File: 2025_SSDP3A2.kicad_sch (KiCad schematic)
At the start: 63 parts, among them J1 SolderPad, J2 SolderPad, J3 SolderPad, J4 SolderPad, Q1 CSD19534Q5A, Q2 BSC0805LS, U1 LM5146RGYR

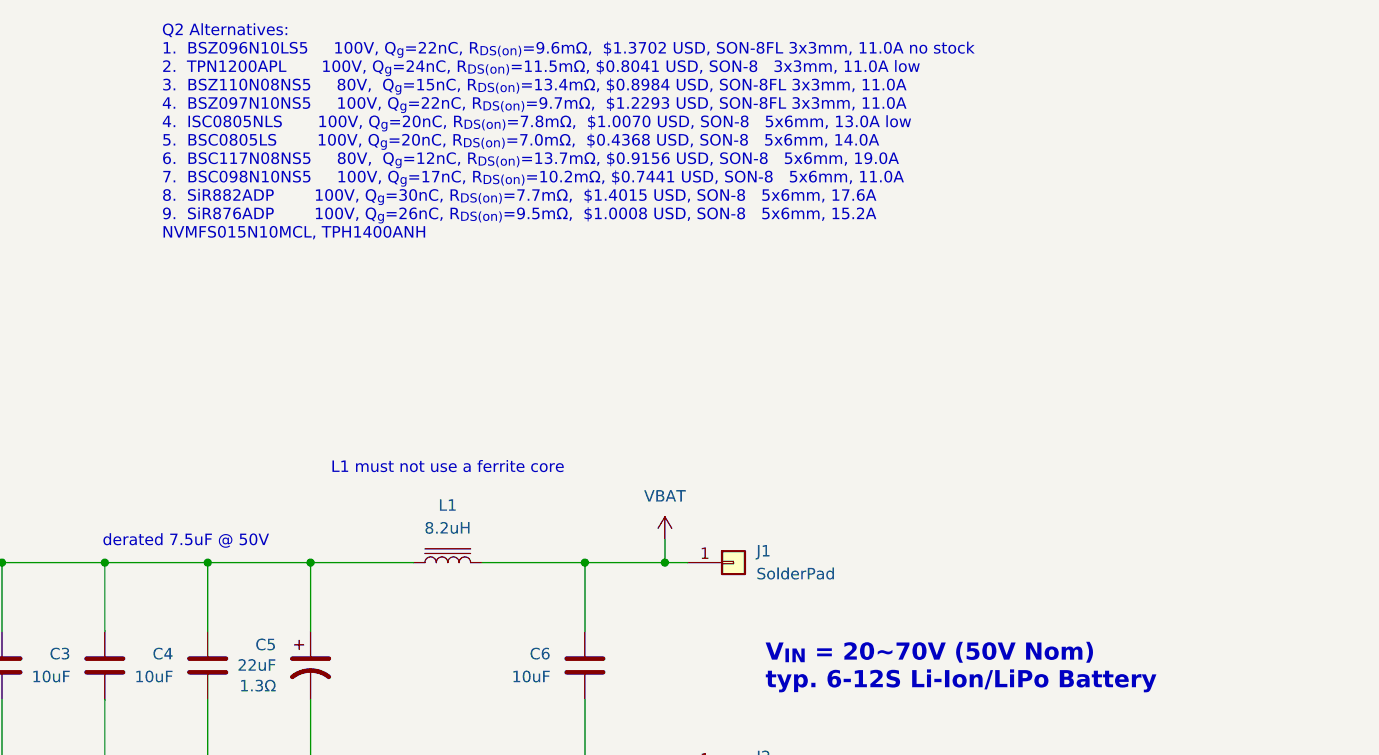
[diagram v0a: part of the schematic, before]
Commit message: Revised PCB layout
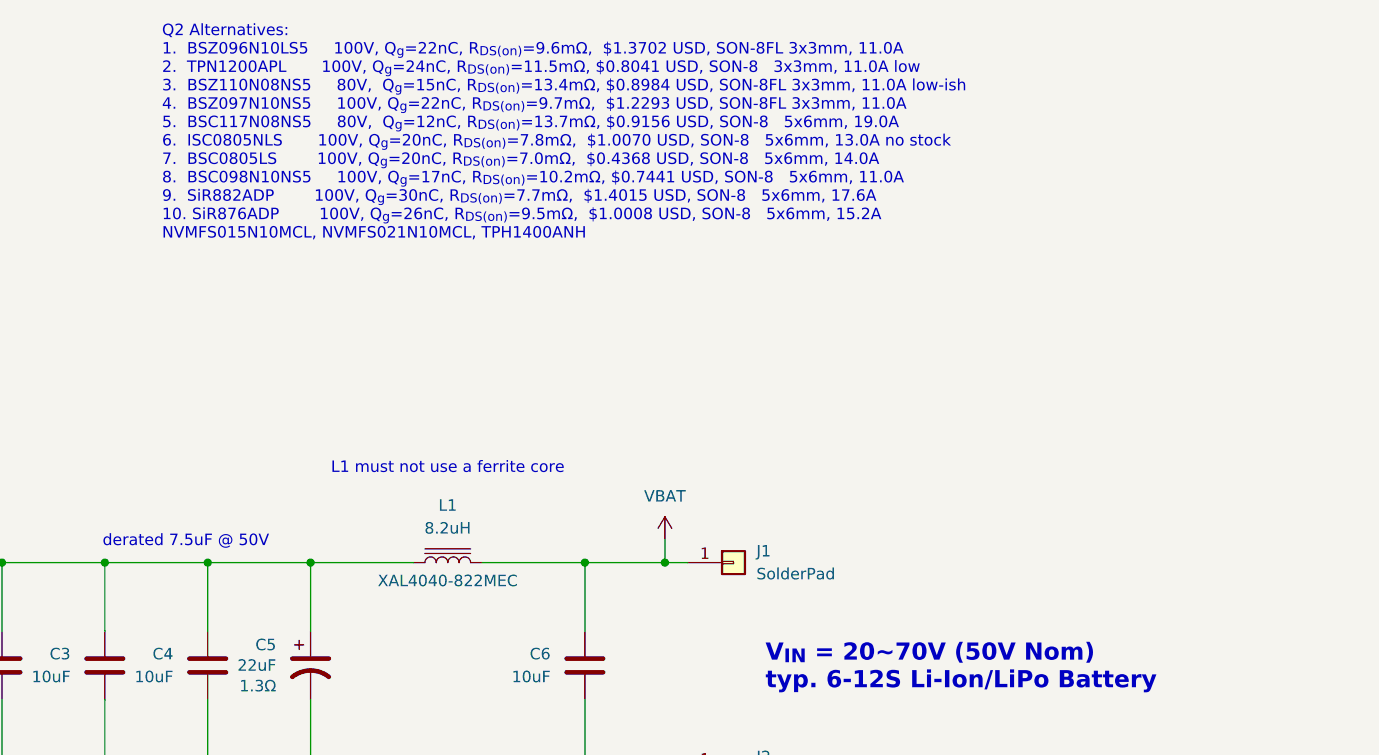
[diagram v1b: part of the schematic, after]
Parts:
- L1: footprint Inductor_SMD:L_Changjiang_FXL0630 -> Inductor_SMD:L_Coilcraft_XAL4040-XXX; LCSC PN C167222 -> C19191624
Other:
- note added: "Q2 Alternatives: 1. BSZ096N10LS5 100V, Q_{g}=22nC, R_{DS(on)}=9.6mΩ, $1.3702 USD, SON-8FL 3x3mm, 11.0A 2. TPN1200APL 100V, Q_{g}=24nC, R_{DS(on)}=11.5mΩ, $0.8041 USD, SON-8 3x3mm, 11.0A low 3. BSZ110N08NS5 80V, Q_{g}=15nC, R_{DS(on)}=13.4mΩ, $0.8984 USD, SON-8FL 3x3mm, 11.0A low-ish 4. BSZ097N10NS5 100V, Q_{g}=22nC, R_{DS(on)}=9.7mΩ, $1.2293 USD, SON-8FL 3x3mm, 11.0A 5. BSC117N08NS5 80V, Q_{g}=12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"
- note removed: "Q2 Alternatives: 1. BSZ096N10LS5 100V, Q_{g}=22nC, R_{DS(on)}=9.6mΩ, $1.3702 USD, SON-8FL 3x3mm, 11.0A no stock 2. TPN1200APL 100V, Q_{g}=24nC, R_{DS(on)}=11.5mΩ, $0.8041 USD, SON-8 3x3mm, 11.0A low 3. BSZ110N08NS5 80V, Q_{g}=15nC, R_{DS(on)}=13.4mΩ, $0.8984 USD, SON-8FL 3x3mm, 11.0A 4. BSZ097N10NS5 100V, Q_{g}=22nC, R_{DS(on)}=9.7mΩ, $1.2293 USD, SON-8FL 3x3mm, 11.0A 4. ISC0805NLS 100V, Q_{g}=20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"
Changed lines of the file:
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@@
 		)
 	)
-	(text "Q2 Alternatives:\n1.  BSZ096N10LS5     100V, Q_{g}=22nC, R_{DS(on)}=9.6mΩ,  $1.3702 USD, SON-8FL 3x3mm, 11.0A no stock\n2.  TPN1200APL       100V, Q_{g}=24nC, R_{DS(on)}=11.5mΩ, $0.8041 USD, SON-8   3x3mm, 11.0A low\n3.  BSZ110N08NS5     80V,  Q_{g}=15nC, R_{DS(on)}=13.4mΩ, $0.8984 USD, SON-8FL 3x3mm, 11.0A\n4.  BSZ097N10NS5     100V, Q_{g}=22nC, R_{DS(on)}=9.7mΩ,  $1.2293 USD, SON-8FL 3x3mm, 11.0A\n4.  ISC0805NLS       100V, Q_{g}=20nC, R_{DS(on)}=7.8mΩ,  $1.0070 USD, SON-8   5x6mm, 13.0A low\n5.  BSC0805LS        100V, Q_{g}=20nC, R_{DS(on)}=7.0mΩ,  $0.4368 USD, SON-8   5x6mm, 14.0A\n6.  BSC117N08NS5     80V,  Q_{g}=12nC, R_{DS(on)}=13.7mΩ, $0.9156 USD, SON-8   5x6mm, 19.0A\n7.  BSC098N10NS5     100V, Q_{g}=17nC, R_{DS(on)}=10.2mΩ, $0.7441 USD, SON-8   5x6mm, 11.0A\n8.  SiR882ADP        100V, Q_{g}=30nC, R_{DS(on)}=7.7mΩ,  $1.4015 USD, SON-8   5x6mm, 17.6A\n9.  SiR876ADP        100V, Q_{g}=26nC, R_{DS(on)}=9.5mΩ,  $1.0008 USD, SON-8   5x6mm, 15.2A\nNVMFS015N10MCL, TPH1400ANH"
+	(text "Q2 Alternatives:\n1.  BSZ096N10LS5     100V, Q_{g}=22nC, R_{DS(on)}=9.6mΩ,  $1.3702 USD, SON-8FL 3x3mm, 11.0A\n2.  TPN1200APL       100V, Q_{g}=24nC, R_{DS(on)}=11.5mΩ, $0.8041 USD, SON-8   3x3mm, 11.0A low\n3.  BSZ110N08NS5     80V,  Q_{g}=15nC, R_{DS(on)}=13.4mΩ, $0.8984 USD, SON-8FL 3x3mm, 11.0A low-ish\n4.  BSZ097N10NS5     100V, Q_{g}=22nC, R_{DS(on)}=9.7mΩ,  $1.2293 USD, SON-8FL 3x3mm, 11.0A\n5.  BSC117N08NS5     80V,  Q_{g}=12nC, R_{DS(on)}=13.7mΩ, $0.9156 USD, SON-8   5x6mm, 19.0A\n6.  ISC0805NLS       100V, Q_{g}=20nC, R_{DS(on)}=7.8mΩ,  $1.0070 USD, SON-8   5x6mm, 13.0A no stock\n7.  BSC0805LS        100V, Q_{g}=20nC, R_{DS(on)}=7.0mΩ,  $0.4368 USD, SON-8   5x6mm, 14.0A\n8.  BSC098N10NS5     100V, Q_{g}=17nC, R_{DS(on)}=10.2mΩ, $0.7441 USD, SON-8   5x6mm, 11.0A\n9.  SiR882ADP        100V, Q_{g}=30nC, R_{DS(on)}=7.7mΩ,  $1.4015 USD, SON-8   5x6mm, 17.6A\n10. SiR876ADP        100V, Q_{g}=26nC, R_{DS(on)}=9.5mΩ,  $1.0008 USD, SON-8   5x6mm, 15.2A\nNVMFS015N10MCL, NVMFS021N10MCL, TPH1400ANH"
 		(exclude_from_sim no)
 		(at 254 25.4 0)
@@
 		(on_board yes)
 		(dnp no)
-		(fields_autoplaced yes)
 		(property "Reference" "L1"
 			(at 285.75 78.74 90)
@@
 			)
 		)
-		(property "Footprint" "Inductor_SMD:L_Changjiang_FXL0630"
+		(property "Footprint" "Inductor_SMD:L_Coilcraft_XAL4040-XXX"
 			(at 285.75 85.09 0)
 			(effects
@@
 			)
 		)
-		(property "Description" "FXL0630-8R2-M"
-			(at 285.75 85.09 0)
+		(property "Description" "XAL4040-822MEC"
+			(at 285.75 87.122 90)
 			(effects
 				(font
 					(size 1.27 1.27)
 				)
-				(hide yes)
 			)
 		)
@@
 			)
 		)
-		(property "LCSC PN" "C167222"
+		(property "LCSC PN" "C19191624"
 			(at 285.75 85.09 90)
 			(effects

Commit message: Note to change iLim
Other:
- note added: "CHANGE THIS! I_{LIM} = 10.2A @ 5V I_{LIM} = 11.2A @ 12V"
- note removed: "I_{LIM} = 10.2A @ 5V I_{LIM} = 11.2A @ 12V"
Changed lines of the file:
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@@
 		)
 	)
-	(text "I_{LIM} = 10.2A @ 5V\nI_{LIM} = 11.2A @ 12V"
+	(text "CHANGE THIS!\nI_{LIM} = 10.2A @ 5V\nI_{LIM} = 11.2A @ 12V"
 		(exclude_from_sim no)
 		(at 182.626 133.858 0)

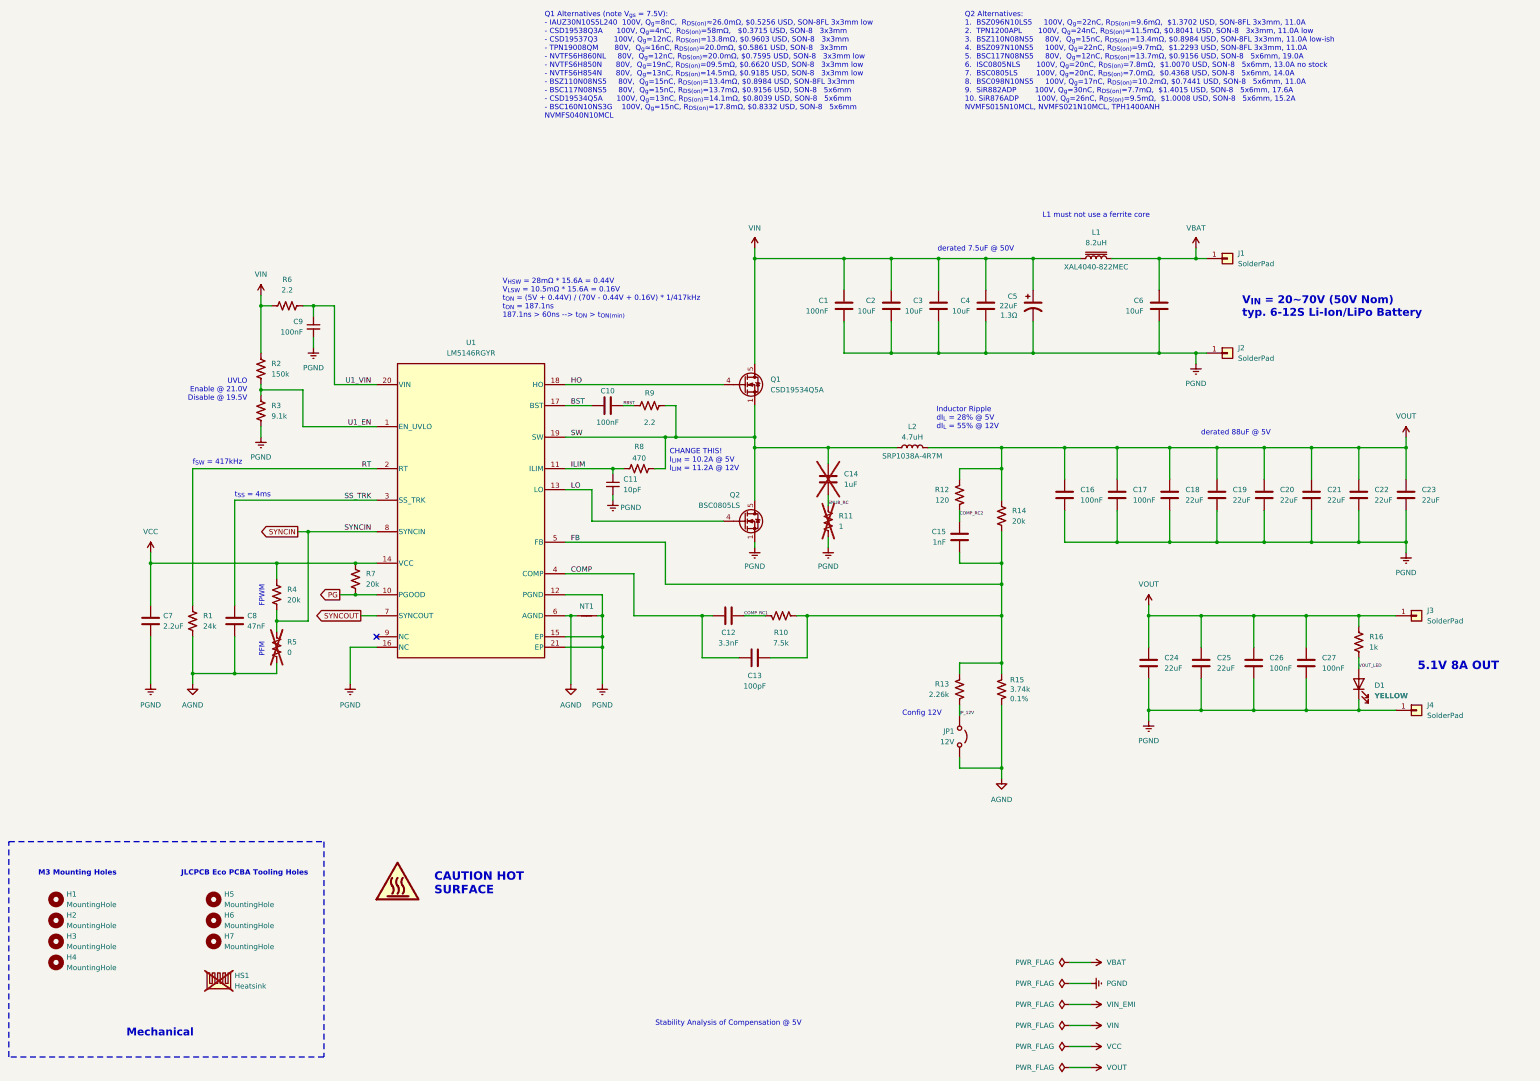
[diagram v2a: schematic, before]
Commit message: Revised PCB layout
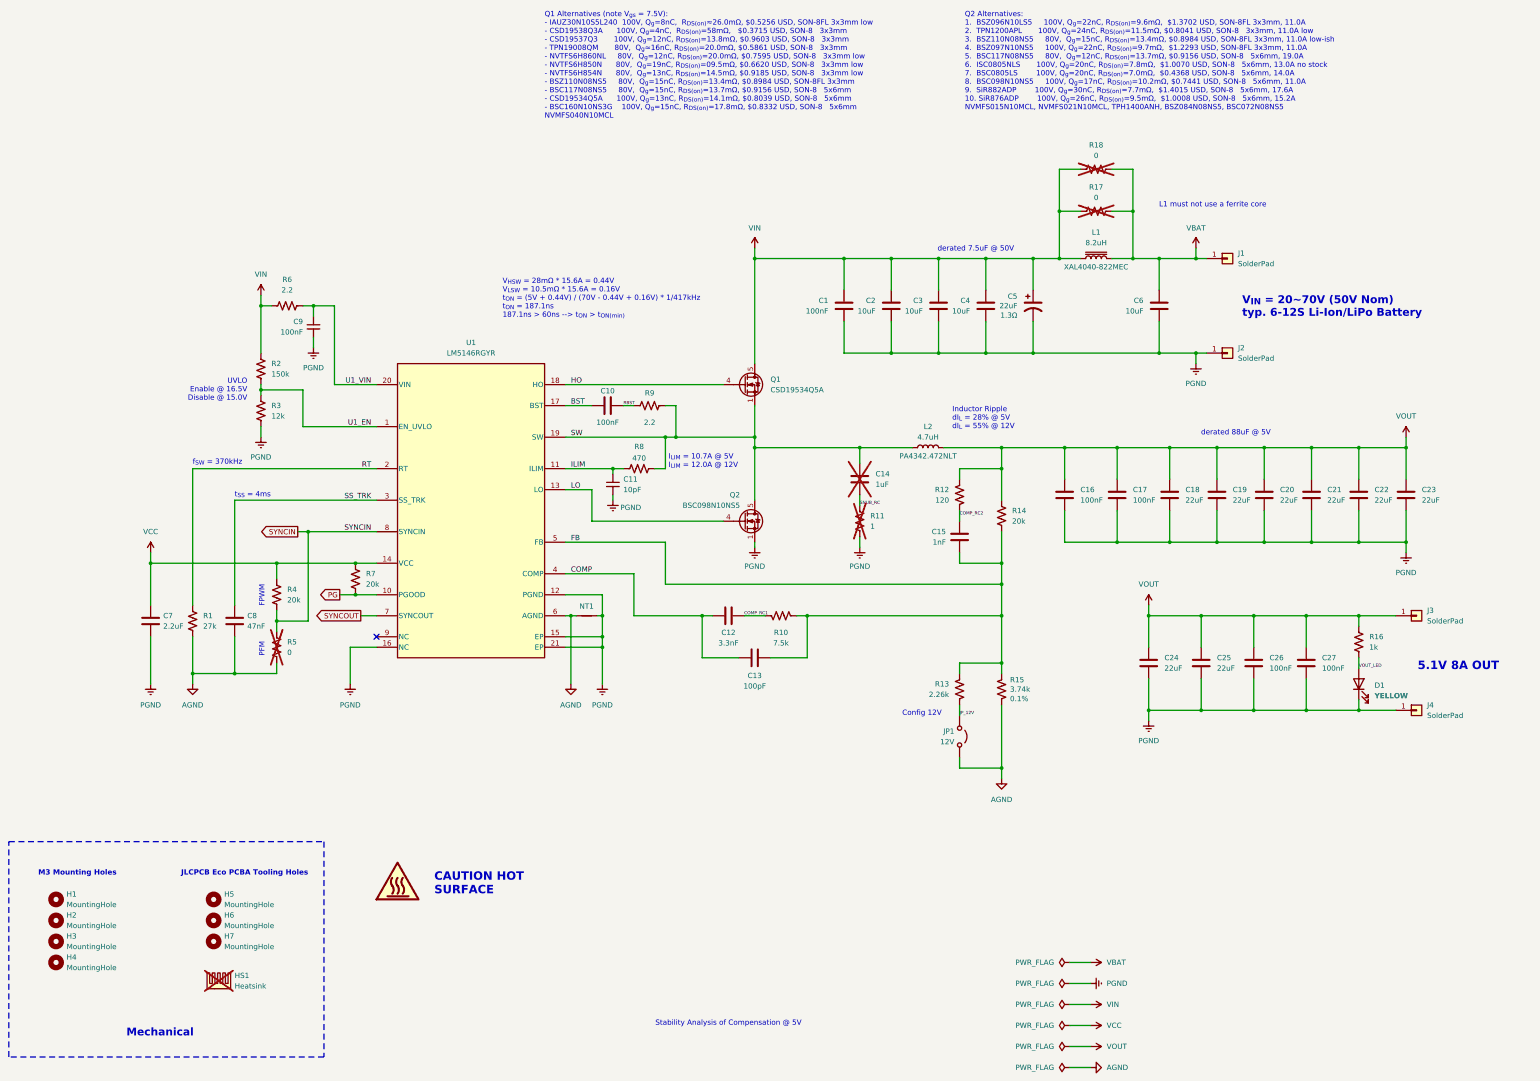
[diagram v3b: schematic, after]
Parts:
- added R17, R18: 0, Resistor_SMD:R_2010_5025Metric, symbol Device:R_US
- L2: footprint Inductor_SMD:L_Bourns_SRP1038C_10.0x10.0mm -> PA4342-472NLT:IND_PA4342_PUL-M; LCSC PN C2041319 -> C6949325
- Q2: value BSC0805LS -> BSC098N10NS5; LCSC PN C534374 -> C534398
- R1: value 24k -> 27k; LCSC PN C31850 -> C22967
- R3: value 9.1k -> 12k; LCSC PN C23260 -> C22790
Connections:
- net VBAT: now also R17.2, R18.2
- net VIN: now also R17.1, R18.1
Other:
- note added: "I_{LIM} = 10.7A @ 5V I_{LIM} = 12.0A @ 12V"
- note added: "UVLO Enable @ 16.5V Disable @ 15.0V"
- note added: "f_{SW} = 370kHz"
- note removed: "CHANGE THIS! I_{LIM} = 10.2A @ 5V I_{LIM} = 11.2A @ 12V"
- note removed: "UVLO Enable @ 21.0V Disable @ 19.5V"
- note removed: "f_{SW} = 417kHz"
- moved on the sheet: C14, L2, R11

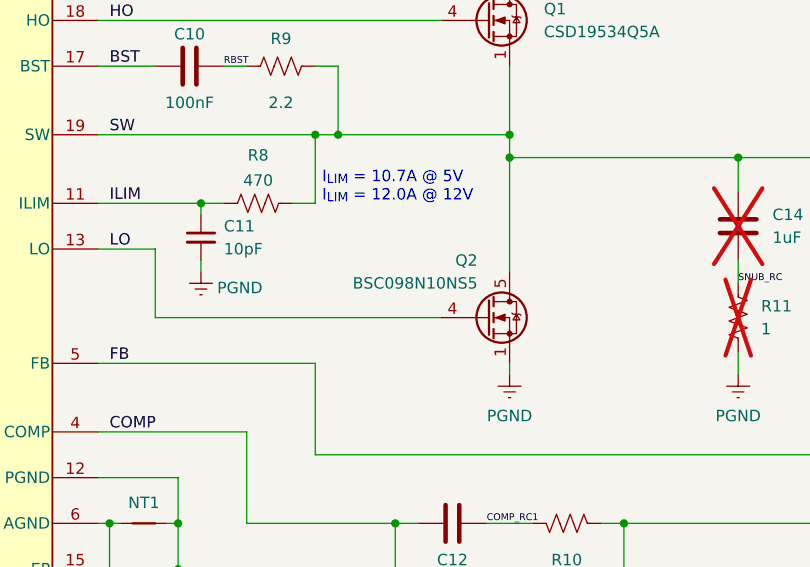
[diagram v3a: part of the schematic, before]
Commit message: Revised MOSFET selection
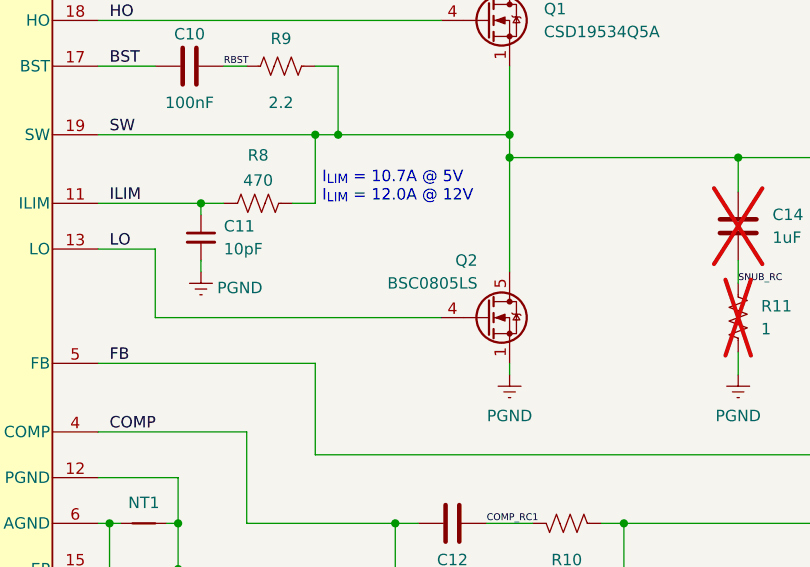
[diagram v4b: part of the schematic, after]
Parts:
- Q2: value BSC098N10NS5 -> BSC0805LS; LCSC PN C534398 -> C534374
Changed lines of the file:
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@@
 			)
 		)
-		(property "Value" "BSC098N10NS5"
+		(property "Value" "BSC0805LS"
 			(at 199.644 144.78 0)
 			(effects
@@
 			)
 		)
-		(property "Datasheet" "https://www.infineon.com/part/BSC098N10NS5"
+		(property "Datasheet" "https://www.infineon.com/part/BSC0805LS"
 			(at 205.74 152.4 0)
 			(effects
@@
 			)
 		)
-		(property "Description" "BSC098N10NS5"
+		(property "Description" "BSC0805LS"
 			(at 200.66 148.59 0)
 			(effects
@@
 			)
 		)
-		(property "LCSC PN" "C534398"
+		(property "LCSC PN" "C534374"
 			(at 200.66 148.59 0)
 			(effects
